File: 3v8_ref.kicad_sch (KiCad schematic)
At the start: 9 parts

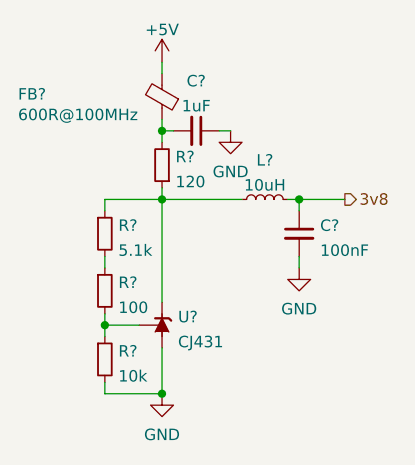
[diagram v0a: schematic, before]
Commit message: Fix broken SPI net labels
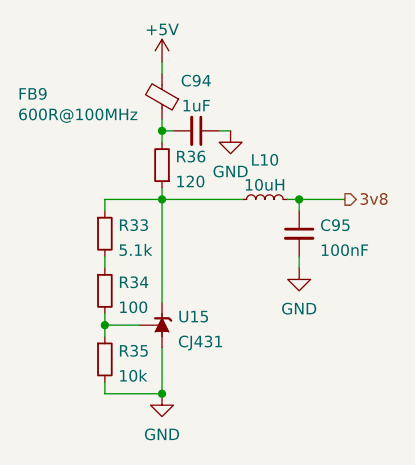
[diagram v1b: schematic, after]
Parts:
- gave numbers to parts that had none: 9
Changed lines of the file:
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@@
   (symbol (lib_id "power:GND") (at 82.55 107.95 0)
     (in_bom yes) (on_board yes) (fields_autoplaced)
-    (property "Reference" "#PWR?" (id 0) (at 82.55 114.3 0)
+    (property "Reference" "#PWR0215" (id 0) (at 82.55 114.3 0)
       (effects (font (size 1.27 1.27)) hide)
     )
@@
   (symbol (lib_id "power:GND") (at 90.17 78.74 0)
     (in_bom yes) (on_board yes) (fields_autoplaced)
-    (property "Reference" "#PWR?" (id 0) (at 90.17 85.09 0)
+    (property "Reference" "#PWR0214" (id 0) (at 90.17 85.09 0)
       (effects (font (size 1.27 1.27)) hide)
     )
@@
   (symbol (lib_id "power:GND") (at 97.79 93.98 0)
     (in_bom yes) (on_board yes) (fields_autoplaced)
-    (property "Reference" "#PWR?" (id 0) (at 97.79 100.33 0)
+    (property "Reference" "#PWR0217" (id 0) (at 97.79 100.33 0)
       (effects (font (size 1.27 1.27)) hide)
     )
@@
   (symbol (lib_id "Device:R_Small") (at 76.2 96.52 0)
     (in_bom yes) (on_board yes) (fields_autoplaced)
-    (property "Reference" "R?" (id 0) (at 77.6986 95.6115 0)
+    (property "Reference" "R34" (id 0) (at 77.6986 95.6115 0)
       (effects (font (size 1.27 1.27)) (justify left))
     )
@@
   (symbol (lib_id "Device:R_Small") (at 76.2 90.17 0)
     (in_bom yes) (on_board yes) (fields_autoplaced)
-    (property "Reference" "R?" (id 0) (at 77.6986 89.2615 0)
+    (property "Reference" "R33" (id 0) (at 77.6986 89.2615 0)
       (effects (font (size 1.27 1.27)) (justify left))
     )
@@
   (symbol (lib_id "Device:R_Small") (at 82.55 82.55 180)
     (in_bom yes) (on_board yes) (fields_autoplaced)
-    (property "Reference" "R?" (id 0) (at 84.0486 81.6415 0)
+    (property "Reference" "R36" (id 0) (at 84.0486 81.6415 0)
       (effects (font (size 1.27 1.27)) (justify right))
     )
@@
   (symbol (lib_id "Device:R_Small") (at 76.2 104.14 0)
     (in_bom yes) (on_board yes) (fields_autoplaced)
-    (property "Reference" "R?" (id 0) (at 77.6986 103.2315 0)
+    (property "Reference" "R35" (id 0) (at 77.6986 103.2315 0)
       (effects (font (size 1.27 1.27)) (justify left))
     )
@@
   (symbol (lib_id "Device:C_Small") (at 86.36 78.74 270) (mirror x)
     (in_bom yes) (on_board yes) (fields_autoplaced)
-    (property "Reference" "C?" (id 0) (at 86.3536 73.2114 90))
+    (property "Reference" "C94" (id 0) (at 86.3536 73.2114 90))
     (property "Value" "1uF" (id 1) (at 86.3536 75.9865 90))
     (property "Footprint" "Capacitor_SMD:C_0402_1005Metric" (id 2) (at 86.36 78.74 0)
@@
   (symbol (lib_id "Device:C_Small") (at 97.79 90.17 0)
     (in_bom yes) (on_board yes) (fields_autoplaced)
-    (property "Reference" "C?" (id 0) (at 100.1141 89.2678 0)
+    (property "Reference" "C95" (id 0) (at 100.1141 89.2678 0)
       (effects (font (size 1.27 1.27)) (justify left))
     )
@@
   (symbol (lib_id "Reference_Voltage:TL431DBZ") (at 82.55 100.33 90)
     (in_bom yes) (on_board yes) (fields_autoplaced)
-    (property "Reference" "U?" (id 0) (at 84.328 99.4215 90)
+    (property "Reference" "U15" (id 0) (at 84.328 99.4215 90)
       (effects (font (size 1.27 1.27)) (justify right))
     )
@@
   (symbol (lib_id "power:+5V") (at 82.55 71.12 0)
     (in_bom yes) (on_board yes) (fields_autoplaced)
-    (property "Reference" "#PWR?" (id 0) (at 82.55 74.93 0)
+    (property "Reference" "#PWR0216" (id 0) (at 82.55 74.93 0)
       (effects (font (size 1.27 1.27)) hide)
     )
@@
   (symbol (lib_id "Device:FerriteBead_Small") (at 82.55 74.93 180)
     (in_bom yes) (on_board yes)
-    (property "Reference" "FB?" (id 0) (at 66.548 74.676 0)
+    (property "Reference" "FB9" (id 0) (at 66.548 74.676 0)
       (effects (font (size 1.27 1.27)) (justify right))
     )
@@
   (symbol (lib_id "Device:L_Small") (at 93.98 86.36 90)
     (in_bom yes) (on_board yes) (fields_autoplaced)
-    (property "Reference" "L?" (id 0) (at 93.98 82.0125 90))
+    (property "Reference" "L10" (id 0) (at 93.98 82.0125 90))
     (property "Value" "10uH" (id 1) (at 93.98 84.7876 90))
     (property "Footprint" "Inductor_SMD:L_0805_2012Metric" (id 2) (at 93.98 86.36 0)

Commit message: Add sensor board power planes
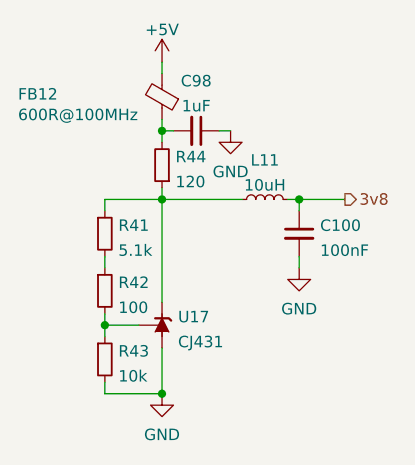
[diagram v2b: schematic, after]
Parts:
- renumbered C95 to C100, C94 to C98, FB9 to FB12, L10 to L11, R33 to R41, R34 to R42, R35 to R43, R36 to R44, U15 to U17
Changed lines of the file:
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@@
   (symbol (lib_id "power:GND") (at 82.55 107.95 0)
     (in_bom yes) (on_board yes) (fields_autoplaced)
-    (property "Reference" "#PWR0215" (id 0) (at 82.55 114.3 0)
+    (property "Reference" "#PWR0226" (id 0) (at 82.55 114.3 0)
       (effects (font (size 1.27 1.27)) hide)
     )
@@
   (symbol (lib_id "power:GND") (at 90.17 78.74 0)
     (in_bom yes) (on_board yes) (fields_autoplaced)
-    (property "Reference" "#PWR0214" (id 0) (at 90.17 85.09 0)
+    (property "Reference" "#PWR0225" (id 0) (at 90.17 85.09 0)
       (effects (font (size 1.27 1.27)) hide)
     )
@@
   (symbol (lib_id "power:GND") (at 97.79 93.98 0)
     (in_bom yes) (on_board yes) (fields_autoplaced)
-    (property "Reference" "#PWR0217" (id 0) (at 97.79 100.33 0)
+    (property "Reference" "#PWR0228" (id 0) (at 97.79 100.33 0)
       (effects (font (size 1.27 1.27)) hide)
     )
@@
   (symbol (lib_id "Device:R_Small") (at 76.2 96.52 0)
     (in_bom yes) (on_board yes) (fields_autoplaced)
-    (property "Reference" "R34" (id 0) (at 77.6986 95.6115 0)
+    (property "Reference" "R42" (id 0) (at 77.6986 95.6115 0)
       (effects (font (size 1.27 1.27)) (justify left))
     )
@@
   (symbol (lib_id "Device:R_Small") (at 76.2 90.17 0)
     (in_bom yes) (on_board yes) (fields_autoplaced)
-    (property "Reference" "R33" (id 0) (at 77.6986 89.2615 0)
+    (property "Reference" "R41" (id 0) (at 77.6986 89.2615 0)
       (effects (font (size 1.27 1.27)) (justify left))
     )
@@
   (symbol (lib_id "Device:R_Small") (at 82.55 82.55 180)
     (in_bom yes) (on_board yes) (fields_autoplaced)
-    (property "Reference" "R36" (id 0) (at 84.0486 81.6415 0)
+    (property "Reference" "R44" (id 0) (at 84.0486 81.6415 0)
       (effects (font (size 1.27 1.27)) (justify right))
     )
@@
   (symbol (lib_id "Device:R_Small") (at 76.2 104.14 0)
     (in_bom yes) (on_board yes) (fields_autoplaced)
-    (property "Reference" "R35" (id 0) (at 77.6986 103.2315 0)
+    (property "Reference" "R43" (id 0) (at 77.6986 103.2315 0)
       (effects (font (size 1.27 1.27)) (justify left))
     )
@@
   (symbol (lib_id "Device:C_Small") (at 86.36 78.74 270) (mirror x)
     (in_bom yes) (on_board yes) (fields_autoplaced)
-    (property "Reference" "C94" (id 0) (at 86.3536 73.2114 90))
+    (property "Reference" "C98" (id 0) (at 86.3536 73.2114 90))
     (property "Value" "1uF" (id 1) (at 86.3536 75.9865 90))
     (property "Footprint" "Capacitor_SMD:C_0402_1005Metric" (id 2) (at 86.36 78.74 0)
@@
   (symbol (lib_id "Device:C_Small") (at 97.79 90.17 0)
     (in_bom yes) (on_board yes) (fields_autoplaced)
-    (property "Reference" "C95" (id 0) (at 100.1141 89.2678 0)
+    (property "Reference" "C100" (id 0) (at 100.1141 89.2678 0)
       (effects (font (size 1.27 1.27)) (justify left))
     )
@@
   (symbol (lib_id "Reference_Voltage:TL431DBZ") (at 82.55 100.33 90)
     (in_bom yes) (on_board yes) (fields_autoplaced)
-    (property "Reference" "U15" (id 0) (at 84.328 99.4215 90)
+    (property "Reference" "U17" (id 0) (at 84.328 99.4215 90)
       (effects (font (size 1.27 1.27)) (justify right))
     )
@@
   (symbol (lib_id "power:+5V") (at 82.55 71.12 0)
     (in_bom yes) (on_board yes) (fields_autoplaced)
-    (property "Reference" "#PWR0216" (id 0) (at 82.55 74.93 0)
+    (property "Reference" "#PWR0227" (id 0) (at 82.55 74.93 0)
       (effects (font (size 1.27 1.27)) hide)
     )
@@
   (symbol (lib_id "Device:FerriteBead_Small") (at 82.55 74.93 180)
     (in_bom yes) (on_board yes)
-    (property "Reference" "FB9" (id 0) (at 66.548 74.676 0)
+    (property "Reference" "FB12" (id 0) (at 66.548 74.676 0)
       (effects (font (size 1.27 1.27)) (justify right))
     )
@@
   (symbol (lib_id "Device:L_Small") (at 93.98 86.36 90)
     (in_bom yes) (on_board yes) (fields_autoplaced)
-    (property "Reference" "L10" (id 0) (at 93.98 82.0125 90))
+    (property "Reference" "L11" (id 0) (at 93.98 82.0125 90))
     (property "Value" "10uH" (id 1) (at 93.98 84.7876 90))
     (property "Footprint" "Inductor_SMD:L_0805_2012Metric" (id 2) (at 93.98 86.36 0)
